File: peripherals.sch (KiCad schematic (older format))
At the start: 57 parts, among them J1 693022010811, J5 U_FL-R-SMT-1_10_, J6 U_FL-R-SMT-1_10_, J7 DM3AT-SF-PEJM5, U6 NCP163ASN330T1G, U7 EMIF06-MSD02N16

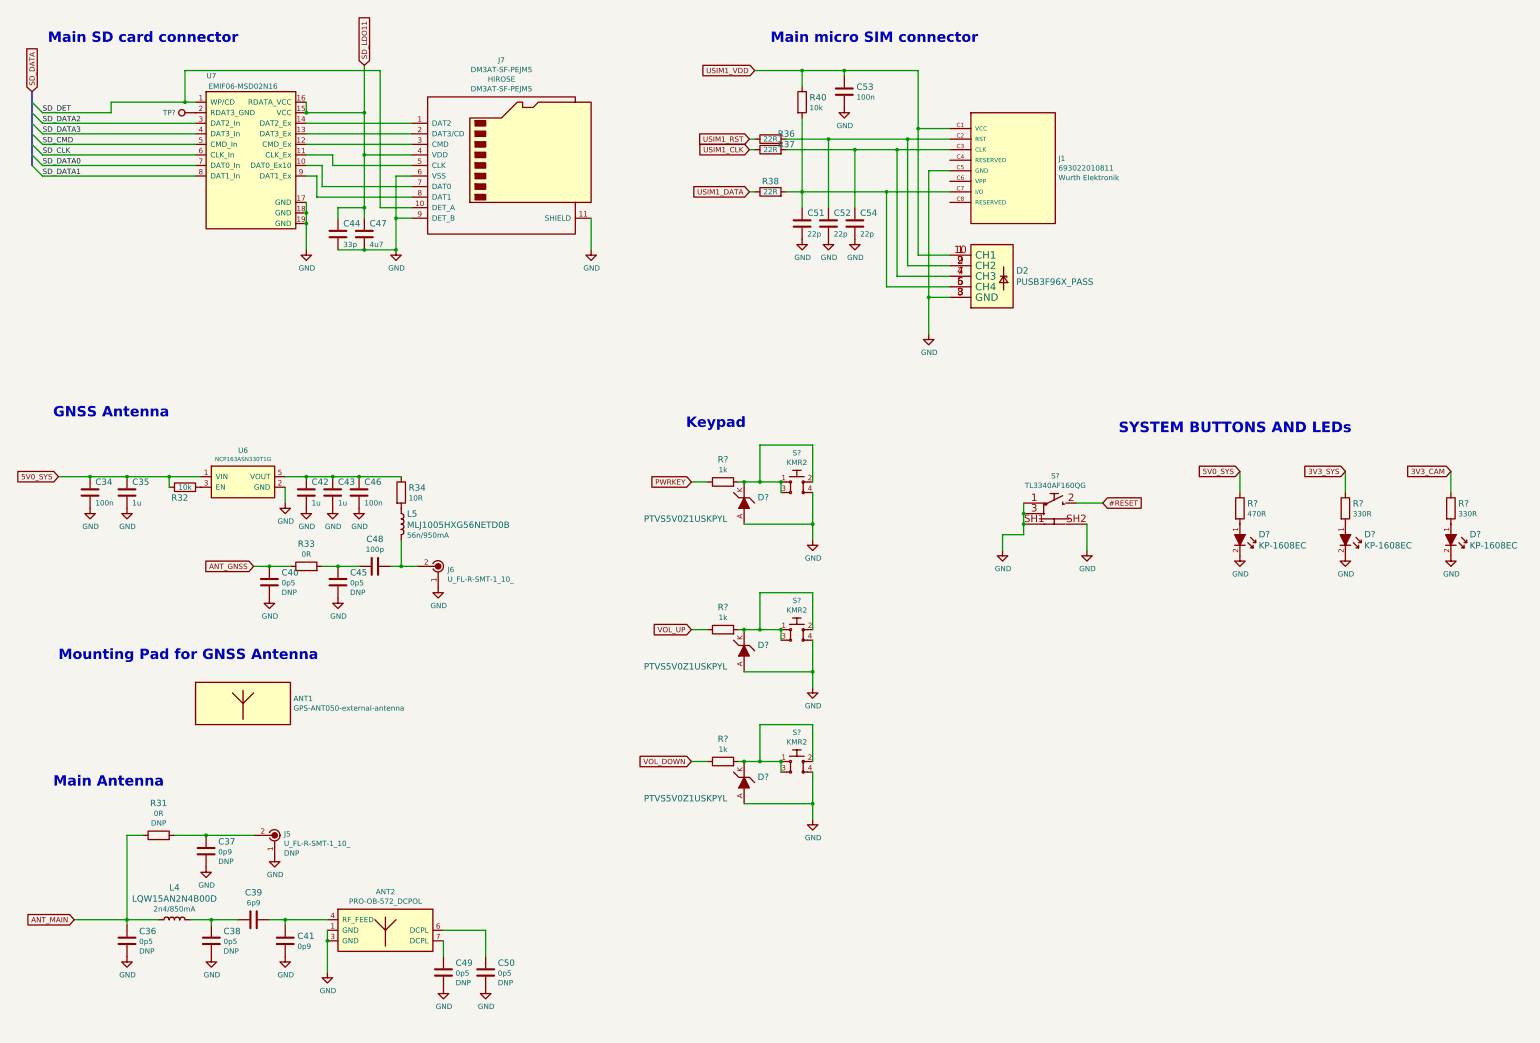
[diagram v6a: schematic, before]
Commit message: Added ESD protection to HDMI
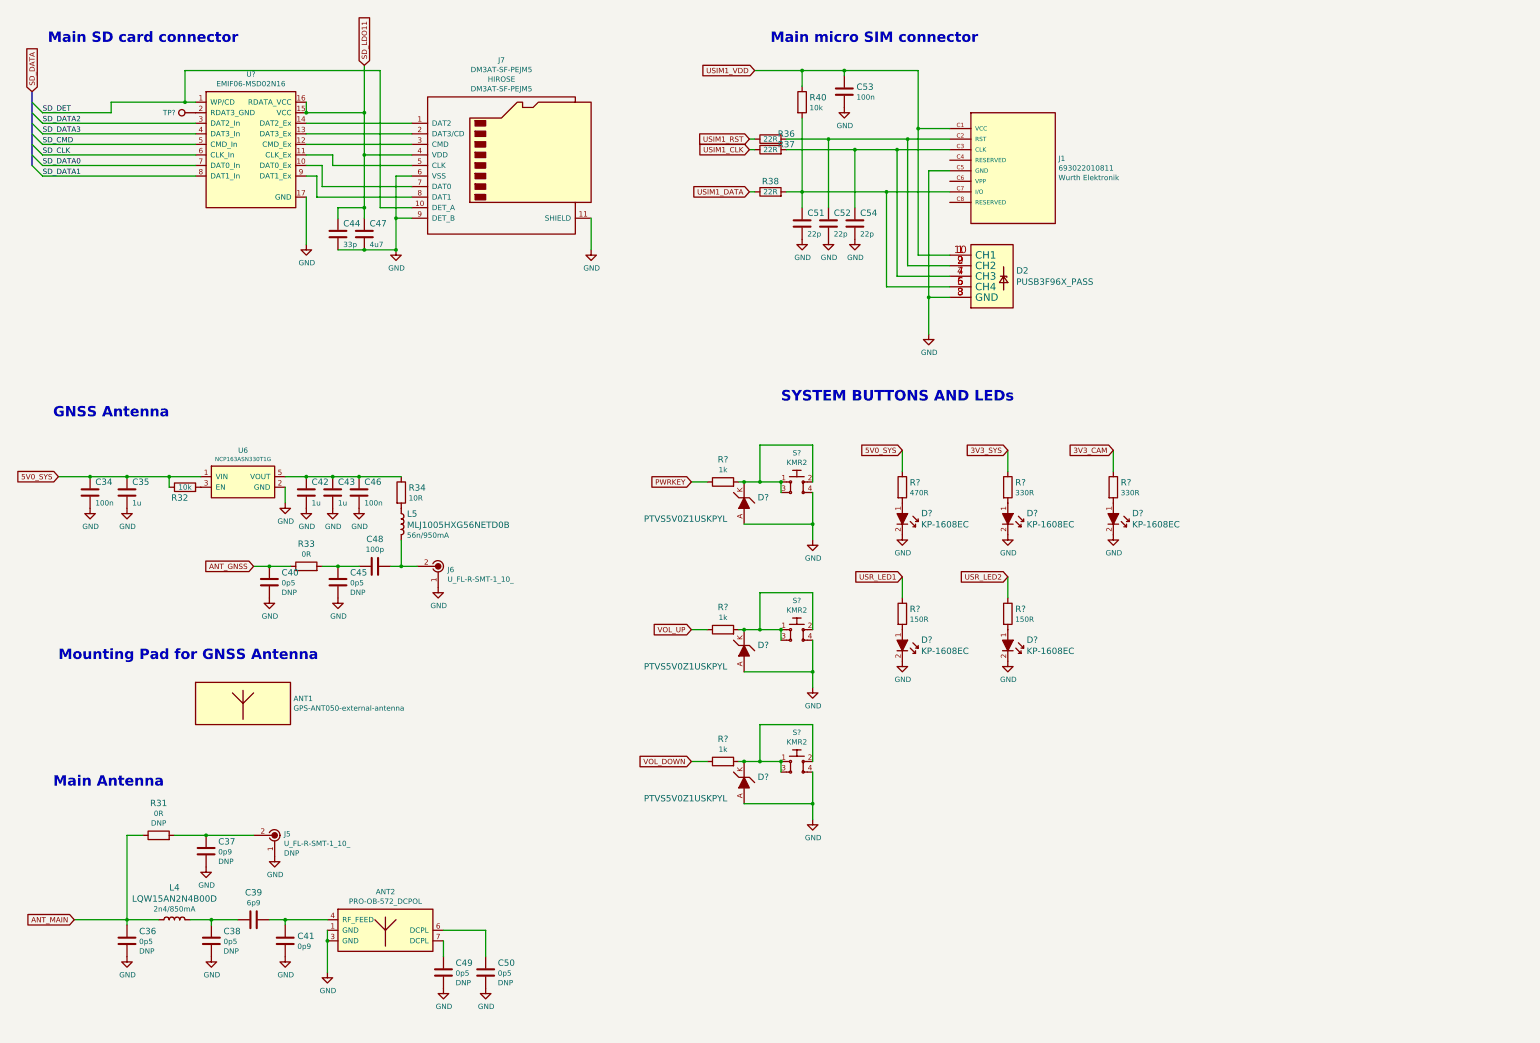
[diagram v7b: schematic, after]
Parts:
- removed S?: TL3340AF160QG, antmicro-footprints:TL3340AF160QG, symbol antmicroPushbuttonSwitches:TL3340AF160QG
- removed U7: EMIF06-MSD02N16, sc606-baseboard-footprints:UFDFN-16_3.5x1.2mm, symbol sc606-baseboard-rescue:EMIF06-MSD02N16-sc606-baseboard
- added D? (x2): KP-1608EC, antmicro-footprints:LED_0603, symbol antmicroLEDIndicationDiscrete:KP-1608EC
- added R? (x2): R_150R_0402, antmicro-footprints:0402-res, symbol antmicroResistors0402:R_150R_0402
- added U?: EMIF06-MSD02N16, sc606-baseboard-footprints:UFDFN-16_3.5x1.2mm, symbol sc606-baseboard:EMIF06-MSD02N16
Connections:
- net GND: now also D?.2, D?.2, U?.17 (GND)
- net SD_CLK: now also U?.6 (CLK_In)
- net SD_CMD: now also U?.5 (CMD_In)
- net SD_DATA0: now also U?.7 (DAT0_In)
- net SD_DATA1: now also U?.8 (DAT1_In)
- net SD_DATA2: now also U?.3 (DAT2_In)
- net SD_DATA3: now also U?.4 (DAT3_In)
- net SD_DET: now also U?.1 (WP/CD)
- net SD_LDO11: now also U?.15 (VCC), U?.16 (RDATA_VCC)
- net at J7.7 (DAT0): now also U?.10 (DAT0_Ex)
- net at J7.5 (CLK): now also U?.11 (CLK_Ex)
- net at J7.3 (CMD): now also U?.12 (CMD_Ex)
- net at J7.2 (DAT3/CD): now also U?.13 (DAT3_Ex)
- net at J7.1 (DAT2): now also U?.14 (DAT2_Ex)
- net at TP?.1: now also U?.2 (RDAT3_GND)
- net at J7.8 (DAT1): now also U?.9 (DAT1_Ex)
- new net: D?.1, R?.2 (x2)
- new net USR_LED1: R?.1
- new net USR_LED2: R?.1
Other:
- note removed: "Keypad"
- moved on the sheet: D?, R?

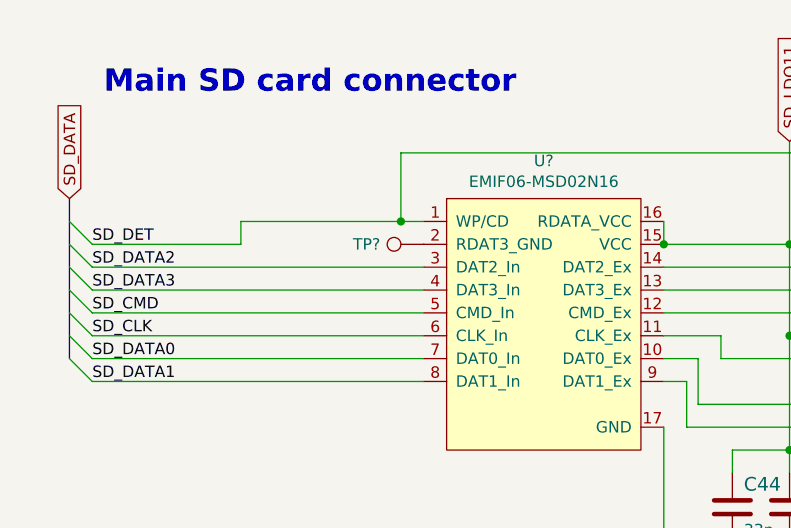
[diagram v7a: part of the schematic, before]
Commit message: Added USB switch along with USB flash connector
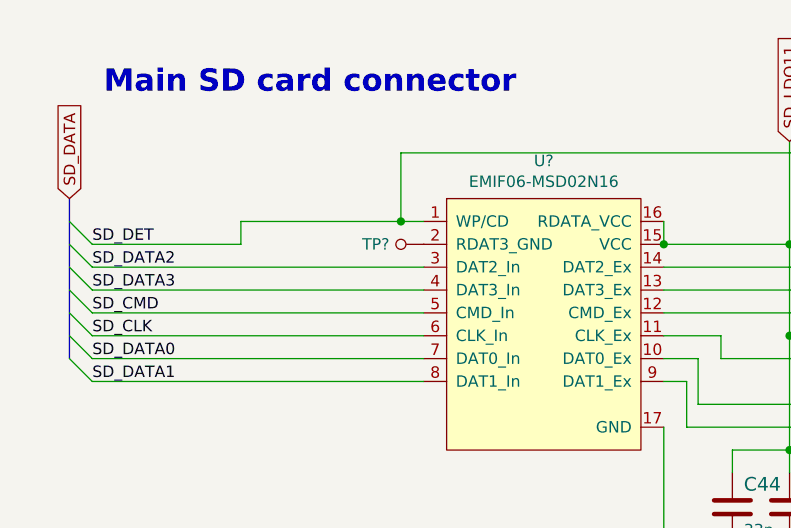
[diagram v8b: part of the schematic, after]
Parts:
- removed TP?: TestPoint, symbol Connector:TestPoint
- added TP?: TP_SMD_0_75MM, antmicro-footprints:Testpoint_smd_0_75mm, symbol antmicroTestPoints:TP_SMD_0_75MM
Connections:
- net at U?.2 (RDAT3_GND): now also TP?.1
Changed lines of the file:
@@
 Wire Wire Line
 	8100 7900 8100 8200
-$Comp
-L Connector:TestPoint TP?
-U 1 1 62632FB3
-P 2250 1650
-F 0 "TP?" V 2250 1900 50  0000 C CNN
-F 1 "TestPoint" V 2354 1722 50  0001 C CNN
-F 2 "" H 2450 1650 50  0001 C CNN
-F 3 "~" H 2450 1650 50  0001 C CNN
-	1    2250 1650
-	0    -1   -1   0
-$EndComp
 Wire Wire Line
 	8950 6250 8950 6050
@@
 $EndComp
 Connection ~ 3300 1650
+$Comp
+L antmicroTestPoints:TP_SMD_0_75MM TP?
+U 1 1 629ACBDB
+P 2150 1650
+F 0 "TP?" V 2150 1600 50  0000 R CNN
+F 1 "TP_SMD_0_75MM" H 2150 1550 50  0001 C CNN
+F 2 "antmicro-footprints:Testpoint_smd_0_75mm" H 2350 1850 60  0001 L CNN
+F 3 "" H 2350 1950 60  0001 L CNN
+	1    2150 1650
+	0    1    1    0
+$EndComp
 Wire Bus Line
 	700  1450 700  2150
